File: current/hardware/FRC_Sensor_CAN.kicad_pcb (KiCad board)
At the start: 4 copper layers, 52 x 64 mm, 124 parts, among them J1 2P PUSH 3.5mm, J2 2P PUSH 3.5mm, J3 2P PUSH 3.5mm, J4 3P PUSH 3.5mm, J5 3P PUSH 3.5mm, J6 3P PUSH 3.5mm, J8 POGO SERVICE, Q1 AO4485, Q101 AO3401A, Q102 BSS138BK, Q201 AO3401A, Q202 BSS138BK, Q301 AO3401A, Q302 BSS138BK, U1 LMR51420XDDCR, U2 AP2112K-3.3, U4 TPS2553DBVR-1, U5 STM32F042K6T6, U6 TCAN3413DR, U7 LM339LV, U8 TPS61085DGKR, U9 TPS2553DBVR-1, Y1 8MHz 18pF

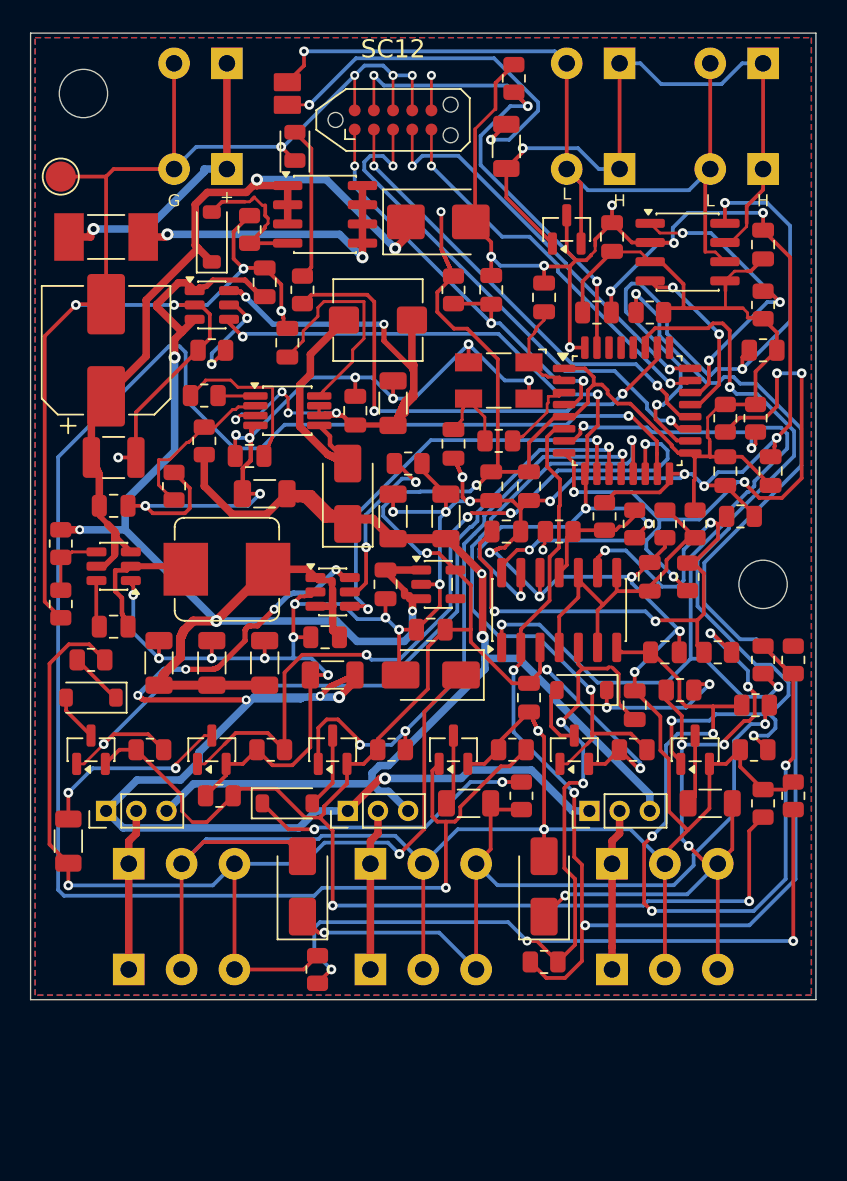
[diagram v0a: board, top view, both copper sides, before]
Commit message: Rev G: protect sensor power and verify startup and fault recovery
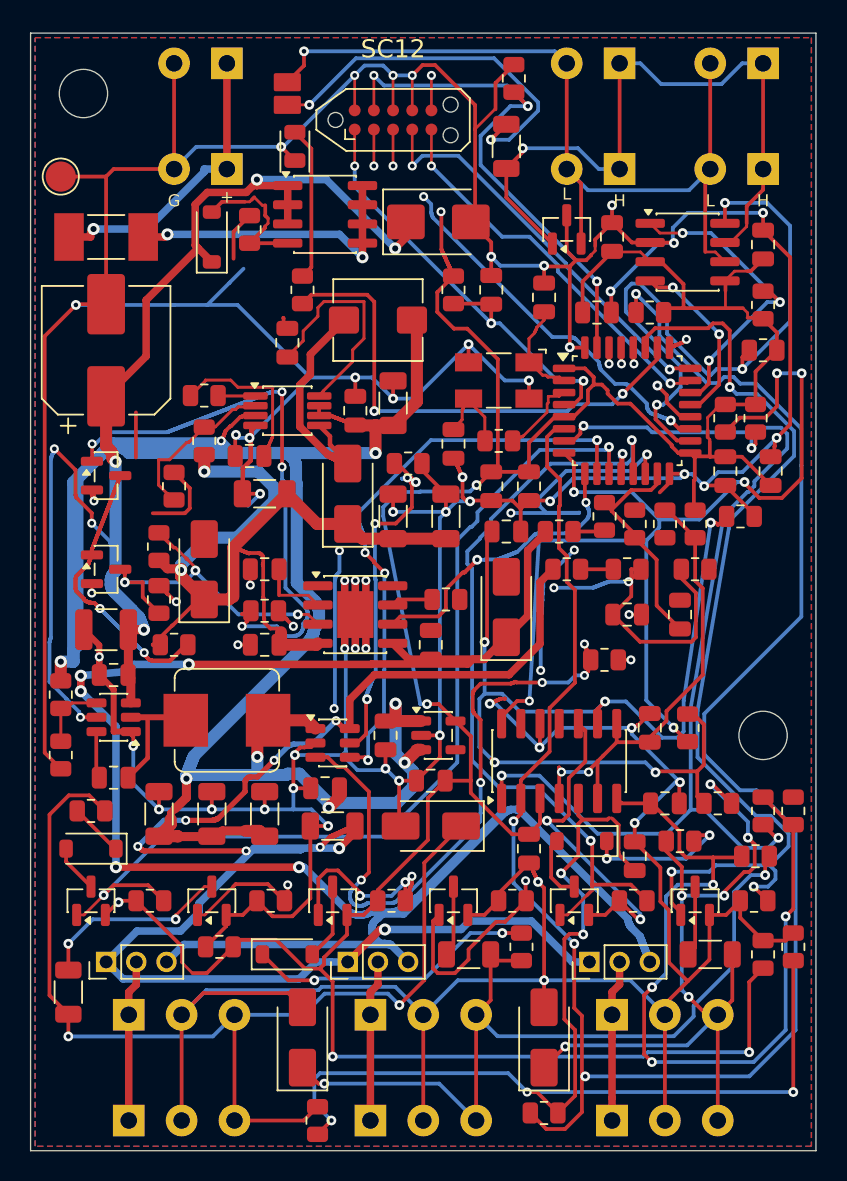
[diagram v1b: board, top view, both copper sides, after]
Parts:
- added C70: 47nF, FRC_Sensor_CAN:C_0805_2012Metric, F.Cu at (15.5, 35.5)
- added C71: 1uF, FRC_Sensor_CAN:C_0805_2012Metric, F.Cu at (26.5, 40.5)
- added C72: 10nF, FRC_Sensor_CAN:C_0805_2012Metric, F.Cu at (43.0, 38.5)
- added C73: 10nF, FRC_Sensor_CAN:C_0805_2012Metric, F.Cu at (39.5, 38.5)
- added D5: B240A, FRC_Sensor_CAN:D_SMA, F.Cu at (31.5, 38.0)
- added D6: SMAJ13A, FRC_Sensor_CAN:D_SMA, F.Cu at (11.5, 35.5)
- added Q2: BSS138BK, FRC_Sensor_CAN:SOT-23, F.Cu at (5.00, 35.5)
- added Q3: BSS138BK, FRC_Sensor_CAN:SOT-23, F.Cu at (5.00, 29.3)
- added R68: 100k, FRC_Sensor_CAN:R_0805_2012Metric, F.Cu at (8.50, 34.0)
- added R69: 12.1k, FRC_Sensor_CAN:R_0805_2012Metric, F.Cu at (8.50, 37.5)
- added R70: 100k, FRC_Sensor_CAN:R_0805_2012Metric, F.Cu at (9.50, 40.5)
- added R71: 10k, FRC_Sensor_CAN:R_0805_2012Metric, F.Cu at (38.0, 41.5)
- added R72: 100k, FRC_Sensor_CAN:R_0805_2012Metric, F.Cu at (35.5, 35.5)
- added R73: 100k, FRC_Sensor_CAN:R_0805_2012Metric, F.Cu at (39.5, 35.5)
- added R74: 20k, FRC_Sensor_CAN:R_0805_2012Metric, F.Cu at (44.0, 35.5)
- added R75: 10k, FRC_Sensor_CAN:R_0805_2012Metric, F.Cu at (15.5, 38.2)
- C61, C65: value 100nF -> 1uF
- R62: value 21.5k -> 2.61k
- R66: value 1.8k -> 100k
- R67: value 2.2M -> 20k
- U9: value TPS2553DBVR-1 -> TPS259620DDAR; footprint FRC_Sensor_CAN:SOT-23-6 -> FRC_Sensor_CAN:TPS2596_DDA8
- moved C65 24.0 mm to (15.5, 40.5), turned to 180 degrees
- moved R62 22.6 mm to (27.5, 37.5), turned to 0 degrees
- moved U9 22.6 mm to (21.5, 38.5)
- moved C2 11.4 mm to (5.00, 39.5), turned to 180 degrees
- moved C3 11.2 mm to (5.50, 42.5), turned to 180 degrees
- moved C101 10.0 mm to (40.0, 54.5)
- moved C11 10.0 mm to (19.5, 50.0)
- moved C12 10.0 mm to (20.0, 52.5)
- moved C13 10.0 mm to (15.5, 51.7)
- moved C201 10.0 mm to (42.0, 51.0)
- moved C4 10.0 mm to (8.50, 51.7)
- moved C5 10.0 mm to (12.0, 51.7)
- moved C50 10.0 mm to (33.0, 54.0)
- moved C51 10.0 mm to (41.0, 46.0)
- moved C6 10.0 mm to (5.50, 49.3)
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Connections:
- C60 pad 1: V5_BOOST -> V5_INTERNAL
- C61 pad 1: V5_BOOST -> V5_INTERNAL
- C62 pad 1: SENSOR_12V -> BOOST_12V
- C63 pad 1: SENSOR_12V -> BOOST_12V
- C64 pad 1: SENSOR_12V -> BOOST_12V
- C65 pad 1: V5_INTERNAL -> BOOST_12V
- D4 pad 1: SENSOR_12V -> BOOST_12V
- L2 pad 1: V5_BOOST -> V5_INTERNAL
- R60 pad 1: SENSOR_12V -> BOOST_12V
- R62 pad 1: BOOST_ILIM -> EFUSE_ILM
- R65 pad 2: SENSE_12V -> ADC12_DIV
- R66 pad 1: SENSE_12V -> ADC12_DIV
- R66 pad 2: GND -> ADC_12V
- R67 pad 1: PG_12V -> ADC_12V
- R67 pad 2: SENSE_12V -> GND
- U2 pad 4: unconnected-(U2-NC-Pad4) -> (no net)
- U4 pad 3: V5_INTERNAL -> POWER_5V_EN
- U5 pad 14: BIAS_DOWN1 -> ADC_5V
- U5 pad 15: BIAS_DOWN2 -> ADC_12V
- U5 pad 25: unconnected-(U5-PA15/NC-Pad25) -> POWER_5V_EN
- U5 pad 28: unconnected-(U5-PB5/NC-Pad28) -> BIAS_DOWN1
- U5 pad 29: unconnected-(U5-PB6/NC-Pad29) -> BIAS_DOWN2
- U5 pad 30: unconnected-(U5-PB7/NC-Pad30) -> POWER_12V_EN
- U5 pad 9: PG_12V -> FAULT_12V_N
- U7 pad 10: REF_LOGIC -> +3V3
- U7 pad 11: SENSE_12V -> GND
- U7 pad 13: PG_12V -> (no net)
- U8 pad 3: V5_BOOST -> V5_INTERNAL
- U8 pad 6: V5_BOOST -> V5_INTERNAL
- U8 pad 7: V5_BOOST -> V5_INTERNAL
- U9 pad 1: V5_INTERNAL -> GND
- U9 pad 2: GND -> EFUSE_SS
- U9 pad 3: V5_INTERNAL -> EFUSE_EN
- U9 pad 4: PG_12V -> BOOST_12V
- U9 pad 5: BOOST_ILIM -> SENSOR_12V
- U9 pad 6: V5_BOOST -> FAULT_12V_N
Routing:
- net POWER_12V_EN: track 0.00 -> 70.8 mm, vias 0 -> 5
- net BIAS_DOWN2: track 122.5 -> 51.7 mm
- net POWER_5V_EN: track 0.00 -> 67.6 mm, vias 0 -> 6
- net V5_INTERNAL: track 90.0 -> 156.0 mm, vias 4 -> 8
- net BOOST_12V: track 0.00 -> 58.5 mm, vias 0 -> 2
- net PG_12V: track 54.7 -> 0.00 mm, vias 5 -> 0
- net SENSOR_12V: track 85.8 -> 133.5 mm, vias 3 -> 5
- net ADC_5V: track 0.00 -> 45.4 mm, vias 0 -> 4
- net V5_BOOST: track 44.0 -> 0.00 mm, vias 6 -> 0
- net VIN_PROT: track 54.8 -> 96.3 mm, vias 2 -> 7
- net GND: track 492.4 -> 524.2 mm, vias 49 -> 59
- net EFUSE_INHIBIT: track 0.00 -> 31.5 mm, vias 0 -> 2
- net SENSE3: track 43.9 -> 69.1 mm, vias 4 -> 5
- net EFUSE_EN: track 0.00 -> 22.8 mm, vias 0 -> 3
- net SENSOR_5V: track 89.3 -> 110.6 mm
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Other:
- board size 52 x 64 mm -> 52 x 74 mm
- board text added: "FAULT RESET: CAN SERVICE"
- board text added: "REV G - 3 DIGITAL INPUTS"
- board text removed: "RAIL FAULT: CYCLE INPUT POWER"
- board text removed: "REV F - 3 DIGITAL INPUTS"

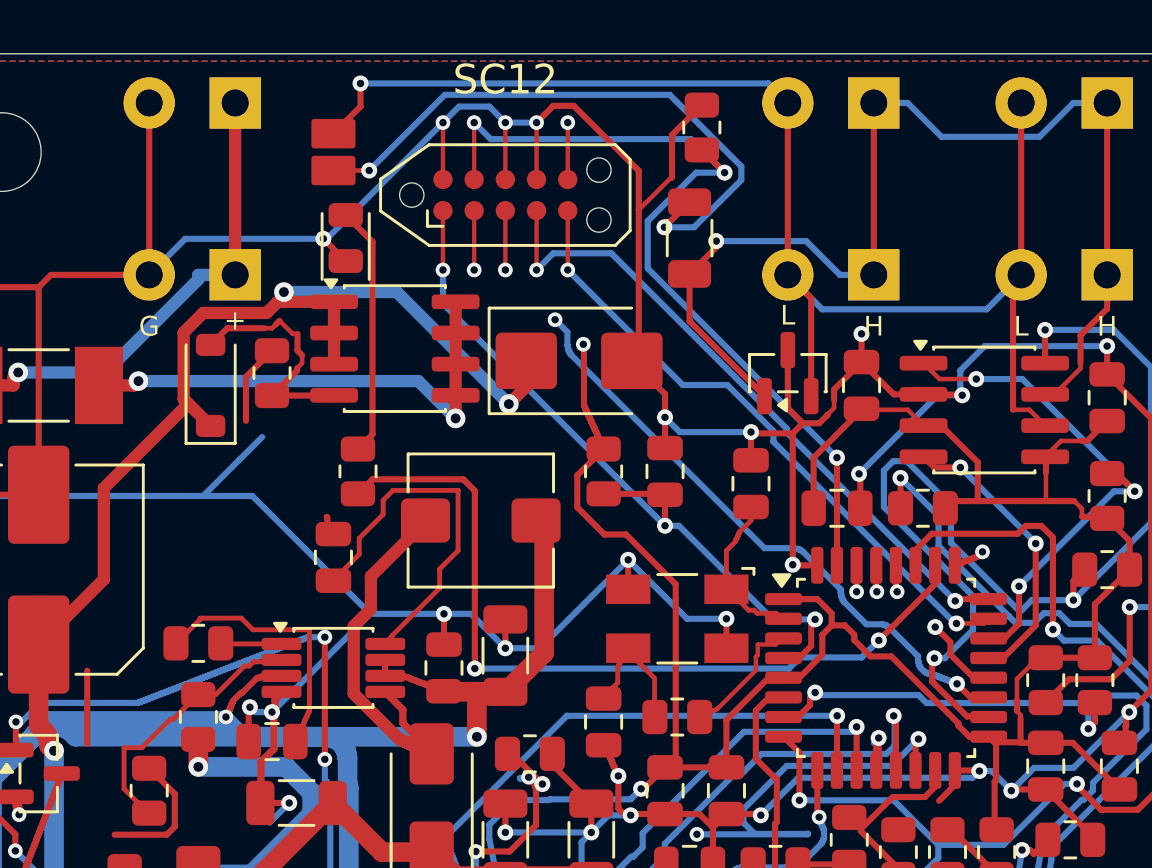
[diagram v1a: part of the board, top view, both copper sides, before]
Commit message: Add Rev H RGB status and low-cost programming header
Keep sensor power and inputs unchanged. Add buffered ARGB status, nonblocking timer/DMA firmware, ordinary hand-fitted SWD header, and updated CAD/BOM/docs. Native and focused firmware checks pass. Explicitly record the canceled full power rerun as incomplete; retain full-release gates and preserve all historical packages.
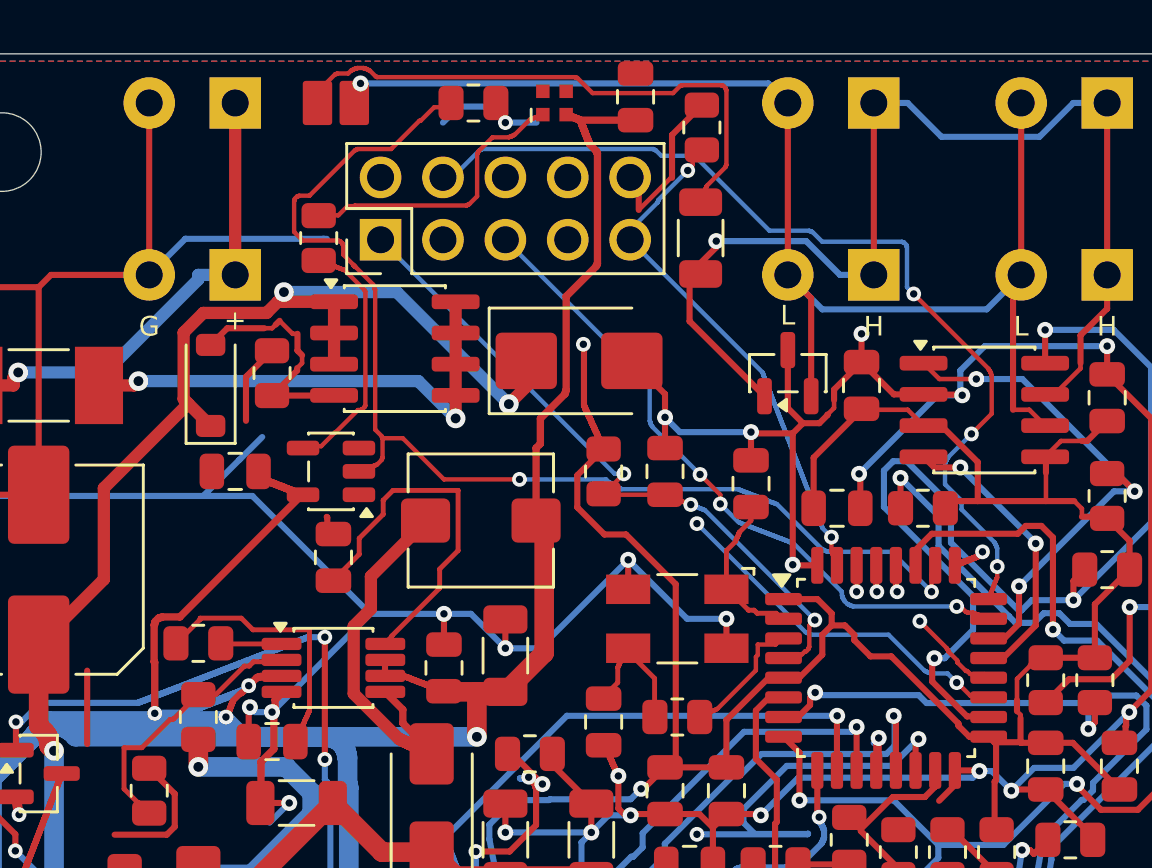
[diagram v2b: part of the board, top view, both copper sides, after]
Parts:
- added C74: 100nF, FRC_Sensor_CAN:C_0805_2012Metric, F.Cu at (13.0, 17.0)
- added C75: 100nF, FRC_Sensor_CAN:C_0805_2012Metric, F.Cu at (29.3, 1.75)
- added R31: 10k, FRC_Sensor_CAN:R_0805_2012Metric, F.Cu at (22.7, 2.00)
- added U10: SN74AHCT1G125, FRC_Sensor_CAN:SOT-23-5, F.Cu at (16.9, 17.0)
- D10: value GREEN -> SK6805-EC15; footprint FRC_Sensor_CAN:LED_0805_2012Metric -> FRC_Sensor_CAN:LED_SK6805_EC15
- J8: value POGO SERVICE -> 2x5 SERVICE 2.54mm; footprint FRC_Sensor_CAN:Tag-Connect_TC2050-IDC-NL_2x05_P1.27mm_Vertical -> FRC_Sensor_CAN:Service_2x05_P2.54mm
- R30: value 1k -> 330
- moved D10 10.1 mm to (26.0, 2.00), turned to 0 degrees
- moved R30 9.63 mm to (16.4, 7.50)
- moved J8 5.40 mm to (18.9, 7.57), turned to 90 degrees
- moved JP2 2.00 mm to (17.1, 2.00), turned to 0 degrees
- moved R42 0.45 mm to (31.9, 7.50)
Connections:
- D10 pad 1: GND -> STATUS_DIN
- D10 pad 2: STATUS_GREEN_A -> V5_INTERNAL
- R30 pad 1: STATUS_GREEN -> STATUS_5V_DATA
- R30 pad 2: STATUS_GREEN_A -> STATUS_DIN
- U5 pad 26: STATUS_GREEN -> STATUS_DATA
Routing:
- net STATUS_DATA: track 0.00 -> 48.3 mm, vias 0 -> 2
- net V5_INTERNAL: track 156.0 -> 196.4 mm, vias 8 -> 10
- net STATUS_GREEN: track 33.4 -> 0.00 mm, vias 2 -> 0
- net GND: track 524.2 -> 497.9 mm, vias 59 -> 56
- net BOOT0: track 35.8 -> 21.6 mm, vias 3 -> 2
- net STATUS_DIN: track 0.00 -> 11.9 mm
- net SWCLK: track 27.1 -> 38.7 mm, vias 2 -> 3
- net STATUS_5V_DATA: track 0.00 -> 10.4 mm
- net STATUS_GREEN_A: track 10.2 -> 0.00 mm
- net UART_RX: track 31.0 -> 35.0 mm, vias 2 -> 1
- net +3V3: track 237.3 -> 234.9 mm, vias 9 -> 8
- net NRST: track 30.5 -> 28.2 mm
- net CAN_TERM: track 25.0 -> 23.2 mm, vias 2 -> 0
- net CANL: track 57.4 -> 55.9 mm
- net SWDIO: track 25.8 -> 27.4 mm, vias 2 -> 3
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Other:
- board text added: "JP2"
- board text added: "REV H - 3 DIGITAL INPUTS"
- board text removed: "REV G - 3 DIGITAL INPUTS"
- board text removed: "SC12"
- board text removed: "TERM 120R"

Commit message: Move RGB LED into reserved right-side light duct area
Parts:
- moved D10 43.5 mm to (48.0, 39.5), turned to 180 degrees
- moved C75 38.6 mm to (48.5, 35.3), turned to 0 degrees
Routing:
- net STATUS_DIN: track 11.9 -> 54.3 mm, vias 0 -> 2
- net V5_INTERNAL: track 196.4 -> 207.9 mm, vias 10 -> 14
- net GND: track 497.9 -> 499.7 mm, vias 56 -> 57
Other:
- board text added: "RGB"

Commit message: Improve edge clearances, recess debug contacts and label wiring
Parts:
- J8: value 2x5 SERVICE 2.54mm -> 2x5 SERVICE SOCKET 2.54mm
- moved R203 13.1 mm to (49.2, 64.5)
- moved R103 8.59 mm to (49.2, 69.0)
- moved R30 6.74 mm to (20.8, 2.40), turned to 0 degrees
- moved R31 3.32 mm to (26.0, 2.40)
- moved R109 1.70 mm to (2.90, 65.2)
- moved R101 1.35 mm to (18.0, 71.1), turned to 0 degrees
- moved JP101 1.10 mm to (5.00, 60.4)
- moved JP201 1.10 mm to (21.0, 60.4)
- moved JP301 1.10 mm to (37.0, 60.4)
- moved F1 0.50 mm to (5.50, 13.5)
- moved R22 0.50 mm to (32.0, 3.50)
- moved Q101 0.30 mm to (4.00, 57.1)
- moved Q201 0.30 mm to (20.0, 57.1)
- moved Q301 0.30 mm to (36.0, 57.1)
- moved D102 0.20 mm to (4.20, 54.0)
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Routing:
- net SENSOR_12V: track 133.5 -> 161.0 mm, vias 5 -> 9
- net SENSE2: track 54.0 -> 71.5 mm
- net BIAS_UP3_N: track 51.5 -> 60.8 mm
- net SENSE1: track 78.3 -> 71.8 mm, vias 5 -> 8
- net STATUS_5V_DATA: track 10.4 -> 16.1 mm
- net SENSOR_5V: track 110.6 -> 115.1 mm, vias 8 -> 10
- net STATUS_DATA: track 48.3 -> 45.0 mm
- net +3V3: track 234.9 -> 238.1 mm, vias 8 -> 10
- net BIAS_SINK1: track 13.0 -> 14.6 mm
- net GND: track 499.7 -> 501.1 mm, vias 57 -> 60
- net VPORT3: track 10.7 -> 11.8 mm
- net VPORT2: track 12.2 -> 13.3 mm
- net VPORT1: track 10.7 -> 11.8 mm
- net BIAS_UP1_N: track 63.5 -> 64.5 mm, vias 2 -> 3
- net BIAS_UP2_N: track 49.4 -> 50.1 mm
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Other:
- board text added: "1"
- board text added: "1 RST / 2 RX / 3 TX / 4 CLK / 5 DIO"
- board text added: "12V"
- board text added: "3V3 = TARGET REFERENCE ONLY"
- board text added: "5V"
- board text added: "6 3V3 / 7 GND / 8 GND / 9 BOOT / 10 GND"
- board text added: "CAN"
- board text added: "CAN A"
- board text added: "CAN B"
- board text added: "DEBUG"
- board text added: "DEBUG: CUSTOM 2x5 PINOUT"
- board text added: "IN1"
- board text added: "IN2"
- board text added: "IN3"
- board text added: "POWER IN"
- board text added: "POWER OFF TO MOVE CAPS"
- board text added: "SC12"
- board text added: "TERM"
- board text added: "TERM 120R"
- board text added: "V1"
- board text added: "V2"
- board text added: "V3"
- board text added: "VIN"
- board text added: "VIN+"
- board text removed: "G"
- board text removed: "JP2"
- board text removed: "P"
- board text removed: "S"
- board text removed: "V+"
